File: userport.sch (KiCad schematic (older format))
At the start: 25 parts, among them CN10 USERPORT, U122 74LS654, U21 74LS04, U22 MOS_6529, U23 MOS_6551_ACIA, U28 GAL16V8, Y2 1.8432M

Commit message: Make JP12 a real jumper
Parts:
- JP12: footprint Jumper:SolderJumper-2_P1.3mm_Bridged_RoundedPad1.0x1.5mm -> Connector_PinHeader_2.54mm:PinHeader_1x02_P2.54mm_Vertical
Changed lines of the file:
@@
 F 0 "JP12" H 13840 1732 50  0000 C CNN
 F 1 "JP_TPSENSE" H 13840 1641 50  0000 C CNN
-F 2 "Jumper:SolderJumper-2_P1.3mm_Bridged_RoundedPad1.0x1.5mm" H 13840 1520 50  0001 C CNN
+F 2 "Connector_PinHeader_2.54mm:PinHeader_1x02_P2.54mm_Vertical" H 13840 1520 50  0001 C CNN
 F 3 "~" H 13840 1520 50  0001 C CNN
 	1    13840 1520

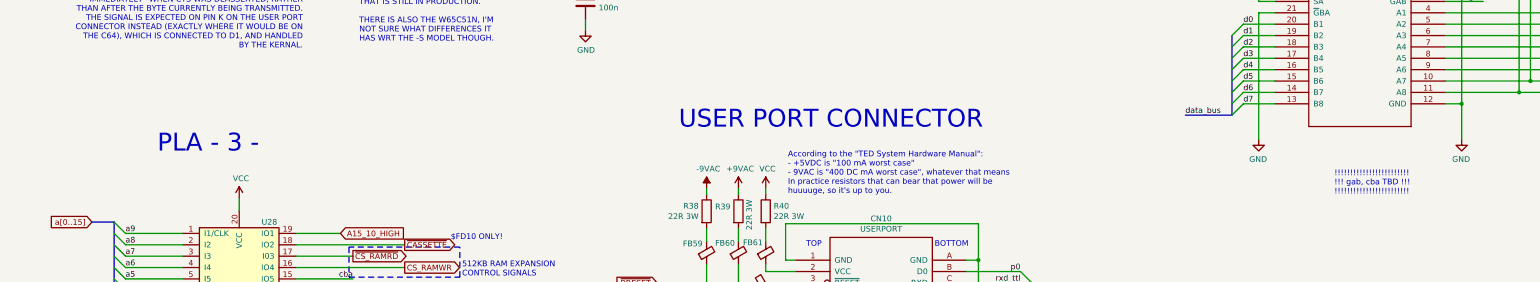
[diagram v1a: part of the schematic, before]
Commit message: Switch to 2-pin header for joyswap
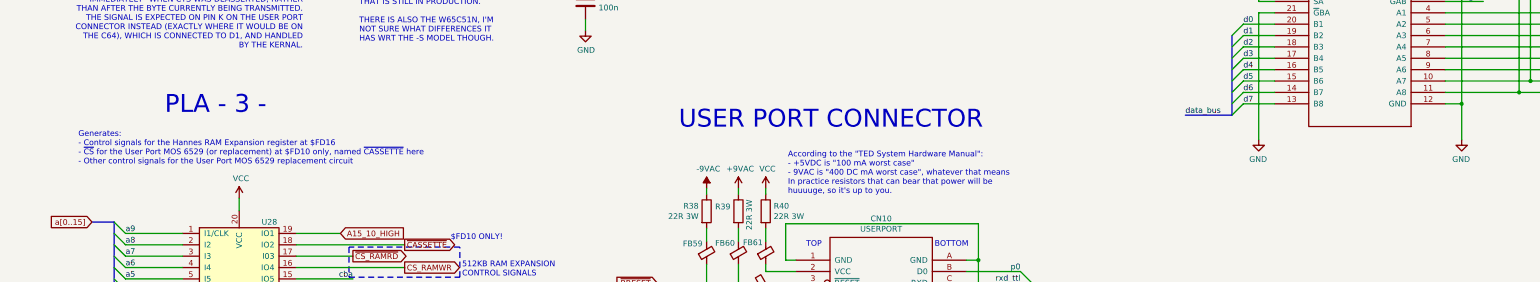
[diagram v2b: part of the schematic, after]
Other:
- note added: "Generates:\n- Control signals for the Hannes RAM Expansion register at $FD16\n- ~CS~ for the User Port MOS 6529 (or replacement) at $FD10 only, named ~CASSETTE~ here\n- Other control signals for the User Port MOS 6529 replacement circuit"
- note removed: "!!!!!!!!!!!!!!!!!!!!!!!!\n!!! gab, cba TBD !!!\n!!!!!!!!!!!!!!!!!!!!!!!!"
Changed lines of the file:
@@
 Text Label 9665 7530 2    50   ~ 0
 txd_ttl
-Text Notes 12425 5960 0    50   ~ 0
-!!!!!!!!!!!!!!!!!!!!!!!!\n!!! gab, cba TBD !!!\n!!!!!!!!!!!!!!!!!!!!!!!!
 Text Notes 8255 4200 0    50   ~ 0
 SOME CONTROL SIGNALS ARE INVERTED FOR\nHISTORICAL REASONS THAT DATE BACK TO\nTHE VIC-1011A
@@
 Text Label 3245 2925 0    50   ~ 0
 q-
-Text Notes 2075 5595 0    157  ~ 0
+Text Notes 2140 5255 0    157  ~ 0
 PLA - 3 -
 Text GLabel 3795 6495 2    50   Output ~ 0
@@
 Wire Bus Line
 	1695 6195 1695 7095
+Text Notes 1380 5695 0    50   ~ 0
+Generates:\n- Control signals for the Hannes RAM Expansion register at $FD16\n- ~CS~ for the User Port MOS 6529 (or replacement) at $FD10 only, named ~CASSETTE~ here\n- Other control signals for the User Port MOS 6529 replacement circuit
 $EndSCHEMATC

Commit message: U21 -> HCT
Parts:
- U21: value 74LS04 -> 74HCT04
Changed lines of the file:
@@
 P 8690 2745
 F 0 "U21" H 8690 2955 50  0000 C CNN
-F 1 "74LS04" H 8700 1605 50  0000 C CNN
+F 1 "74HCT04" H 8700 1605 50  0000 C CNN
 F 2 "LittleSixteen:DIP-14_W7.62mm_Socket_LongPads" H 8690 2745 50  0001 C CNN
 F 3 "http://www.ti.com/lit/gpn/sn74LS04" H 8690 2745 50  0001 C CNN
@@
 P 8690 2340
 F 0 "U21" H 8690 2565 50  0000 C CNN
-F 1 "74LS04" H 8690 2566 50  0001 C CNN
+F 1 "74HCT04" H 8690 2566 50  0001 C CNN
 F 2 "LittleSixteen:DIP-14_W7.62mm_Socket_LongPads" H 8690 2340 50  0001 C CNN
 F 3 "http://www.ti.com/lit/gpn/sn74LS04" H 8690 2340 50  0001 C CNN
@@
 P 8690 3210
 F 0 "U21" H 8690 3435 50  0000 C CNN
-F 1 "74LS04" H 8690 3436 50  0001 C CNN
+F 1 "74HCT04" H 8690 3436 50  0001 C CNN
 F 2 "LittleSixteen:DIP-14_W7.62mm_Socket_LongPads" H 8690 3210 50  0001 C CNN
 F 3 "http://www.ti.com/lit/gpn/sn74LS04" H 8690 3210 50  0001 C CNN
@@
 P 8690 3655
 F 0 "U21" H 8690 3880 50  0000 C CNN
-F 1 "74LS04" H 8690 3881 50  0001 C CNN
+F 1 "74HCT04" H 8690 3881 50  0001 C CNN
 F 2 "LittleSixteen:DIP-14_W7.62mm_Socket_LongPads" H 8690 3655 50  0001 C CNN
 F 3 "http://www.ti.com/lit/gpn/sn74LS04" H 8690 3655 50  0001 C CNN
@@
 P 11070 10770
 F 0 "U21" H 11070 11087 50  0000 C CNN
-F 1 "74LS04" H 11070 10996 50  0000 C CNN
+F 1 "74HCT04" H 11070 10996 50  0000 C CNN
 F 2 "LittleSixteen:DIP-14_W7.62mm_Socket_LongPads" H 11070 10770 50  0001 C CNN
 F 3 "http://www.ti.com/lit/gpn/sn74LS04" H 11070 10770 50  0001 C CNN
@@
 P 2975 10020
 F 0 "U21" H 3205 10066 50  0000 L CNN
-F 1 "74LS04" H 3205 9975 50  0000 L CNN
+F 1 "74HCT04" H 3205 9975 50  0000 L CNN
 F 2 "LittleSixteen:DIP-14_W7.62mm_Socket_LongPads" H 2975 10020 50  0001 C CNN
 F 3 "http://www.ti.com/lit/gpn/sn74LS04" H 2975 10020 50  0001 C CNN

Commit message: Rationalize BOM There should be no significant changes on both schematics on PCB, just some values and something on the silkscreen
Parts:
- C42, C43: MouserPN (none) -> 810-FG28X7R1H104KNT0
- FB59, FB60, FB61, FB62, FB63, FB64, FB65: value Ferrite_Bead_Small -> DSS1NB32A271Q91A; footprint LittleSixteen:Ferrite -> LittleSixteen:EMI_Filter; symbol ferrite_bead_small:Ferrite_Bead_Small -> emi_filter_3pin:EMI_Filter_3Pin
- JP12: value JP_TPSENSE -> JMP_TPSENSE
- R38, R39, R40: value 22R 3W -> 22 3W
- RP4: renamed from RN1; Notes (none) -> Bussed
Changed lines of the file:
@@
 d7
 $Comp
-L Device:R_Network08 RN1
+L Device:R_Network08 RP4
 U 1 1 63F3B9D0
 P 14350 3935
-F 0 "RN1" H 14738 3981 50  0000 L CNN
+F 0 "RP4" H 14738 3981 50  0000 L CNN
 F 1 "8.2k" H 14738 3890 50  0000 L CNN
 F 2 "Resistor_THT:R_Array_SIP9" V 14825 3935 50  0001 C CNN
 F 3 "http://www.vishay.com/docs/31509/csc.pdf" H 14350 3935 50  0001 C CNN
+F 4 "Bussed" H 14350 3935 50  0001 C CNN "Notes"
 	1    14350 3935
 	-1   0    0    -1
@@
 F 2 "Capacitor_THT:C_Disc_D8.0mm_W2.5mm_P5.00mm" H 2438 9890 50  0001 C CNN
 F 3 "~" H 2400 10040 50  0001 C CNN
+F 4 "810-FG28X7R1H104KNT0" H 2400 10040 50  0001 C CNN "MouserPN"
 	1    2400 10040
 	1    0    0    -1
@@
 	6905 7530 6905 6565
 $Comp
-L ferrite_bead_small:Ferrite_Bead_Small FB?
+L emi_filter_3pin:EMI_Filter_3Pin FB?
 U 1 1 647718B2
 P 7390 6730
@@
 AR Path="/63EAD078/647718B2" Ref="FB62"  Part="1"
 F 0 "FB62" V 7335 6595 50  0000 C CNN
-F 1 "Ferrite_Bead_Small" H 7490 6685 50  0001 L CNN
-F 2 "LittleSixteen:Ferrite" V 7320 6730 50  0001 C CNN
+F 1 "DSS1NB32A271Q91A" H 7490 6685 50  0001 L CNN
+F 2 "LittleSixteen:EMI_Filter" V 7320 6730 50  0001 C CNN
 F 3 "~" H 7390 6730 50  0001 C CNN
 	1    7390 6730
@@
 $EndComp
 $Comp
-L ferrite_bead_small:Ferrite_Bead_Small FB?
+L emi_filter_3pin:EMI_Filter_3Pin FB?
 U 1 1 6477BD12
 P 7185 6465
@@
 AR Path="/63EAD078/6477BD12" Ref="FB60"  Part="1"
 F 0 "FB60" H 6980 6380 50  0000 L CNN
-F 1 "Ferrite_Bead_Small" H 7285 6420 50  0001 L CNN
-F 2 "LittleSixteen:Ferrite" V 7115 6465 50  0001 C CNN
+F 1 "DSS1NB32A271Q91A" H 7285 6420 50  0001 L CNN
+F 2 "LittleSixteen:EMI_Filter" V 7115 6465 50  0001 C CNN
 F 3 "~" H 7185 6465 50  0001 C CNN
 	1    7185 6465
@@
 $EndComp
 $Comp
-L ferrite_bead_small:Ferrite_Bead_Small FB?
+L emi_filter_3pin:EMI_Filter_3Pin FB?
 U 1 1 64790452
 P 7455 7760
@@
 AR Path="/63EAD078/64790452" Ref="FB64"  Part="1"
 F 0 "FB64" H 7261 7760 50  0000 R CNN
-F 1 "Ferrite_Bead_Small" H 7555 7715 50  0001 L CNN
-F 2 "LittleSixteen:Ferrite" V 7385 7760 50  0001 C CNN
+F 1 "DSS1NB32A271Q91A" H 7555 7715 50  0001 L CNN
+F 2 "LittleSixteen:EMI_Filter" V 7385 7760 50  0001 C CNN
 F 3 "~" H 7455 7760 50  0001 C CNN
 	1    7455 7760
@@
 $EndComp
 $Comp
-L ferrite_bead_small:Ferrite_Bead_Small FB?
+L emi_filter_3pin:EMI_Filter_3Pin FB?
 U 1 1 647AEC6A
 P 9295 7760
@@
 AR Path="/63EAD078/647AEC6A" Ref="FB65"  Part="1"
 F 0 "FB65" H 9050 7685 50  0000 L CNN
-F 1 "Ferrite_Bead_Small" H 9395 7715 50  0001 L CNN
-F 2 "LittleSixteen:Ferrite" V 9225 7760 50  0001 C CNN
+F 1 "DSS1NB32A271Q91A" H 9395 7715 50  0001 L CNN
+F 2 "LittleSixteen:EMI_Filter" V 9225 7760 50  0001 C CNN
 F 3 "~" H 9295 7760 50  0001 C CNN
 	1    9295 7760
@@
 $EndComp
 $Comp
-L ferrite_bead_small:Ferrite_Bead_Small FB?
+L emi_filter_3pin:EMI_Filter_3Pin FB?
 U 1 1 647B8E58
 P 7425 6465
@@
 AR Path="/63EAD078/647B8E58" Ref="FB61"  Part="1"
 F 0 "FB61" H 7225 6375 50  0000 L CNN
-F 1 "Ferrite_Bead_Small" H 7525 6420 50  0001 L CNN
-F 2 "LittleSixteen:Ferrite" V 7355 6465 50  0001 C CNN
+F 1 "DSS1NB32A271Q91A" H 7525 6420 50  0001 L CNN
+F 2 "LittleSixteen:EMI_Filter" V 7355 6465 50  0001 C CNN
 F 3 "~" H 7425 6465 50  0001 C CNN
 	1    7425 6465
@@
 AR Path="/63EAD078/647C5CFF" Ref="R40"  Part="1"
 F 0 "R40" H 7495 6146 50  0000 L CNN
-F 1 "22R 3W" H 7495 6055 50  0000 L CNN
+F 1 "22 3W" H 7495 6055 50  0000 L CNN
 F 2 "Resistor_THT:R_Axial_DIN0414_L11.9mm_D4.5mm_P5.08mm_Vertical" V 7355 6100 50  0001 C CNN
 F 3 "~" H 7425 6100 50  0001 C CNN
@@
 	7490 7330 7690 7330
 $Comp
-L ferrite_bead_small:Ferrite_Bead_Small FB?
+L emi_filter_3pin:EMI_Filter_3Pin FB?
 U 1 1 6479A5EF
 P 7390 7330
@@
 AR Path="/63EAD078/6479A5EF" Ref="FB63"  Part="1"
 F 0 "FB63" V 7330 7195 50  0000 C CNN
-F 1 "Ferrite_Bead_Small" H 7490 7285 50  0001 L CNN
-F 2 "LittleSixteen:Ferrite" V 7320 7330 50  0001 C CNN
+F 1 "DSS1NB32A271Q91A" H 7490 7285 50  0001 L CNN
+F 2 "LittleSixteen:EMI_Filter" V 7320 7330 50  0001 C CNN
 F 3 "~" H 7390 7330 50  0001 C CNN
 	1    7390 7330
@@
 AR Path="/63EAD078/6486FE58" Ref="JP12"  Part="1"
 F 0 "JP12" H 13840 1732 50  0000 C CNN
-F 1 "JP_TPSENSE" H 13840 1641 50  0000 C CNN
+F 1 "JMP_TPSENSE" H 13840 1641 50  0000 C CNN
 F 2 "Connector_PinHeader_2.54mm:PinHeader_1x02_P2.54mm_Vertical" H 13840 1520 50  0001 C CNN
 F 3 "~" H 13840 1520 50  0001 C CNN
@@
 ~TAPE_SENSE
 $Comp
-L ferrite_bead_small:Ferrite_Bead_Small FB?
+L emi_filter_3pin:EMI_Filter_3Pin FB?
 U 1 1 647EB007
 P 6905 6465
@@
 AR Path="/63EAD078/647EB007" Ref="FB59"  Part="1"
 F 0 "FB59" H 6870 6385 50  0000 R CNN
-F 1 "Ferrite_Bead_Small" H 7005 6420 50  0001 L CNN
-F 2 "LittleSixteen:Ferrite" V 6835 6465 50  0001 C CNN
+F 1 "DSS1NB32A271Q91A" H 7005 6420 50  0001 L CNN
+F 2 "LittleSixteen:EMI_Filter" V 6835 6465 50  0001 C CNN
 F 3 "~" H 6905 6465 50  0001 C CNN
 	1    6905 6465
@@
 AR Path="/63EAD078/64956DD2" Ref="R38"  Part="1"
 F 0 "R38" H 6835 6146 50  0000 R CNN
-F 1 "22R 3W" H 6835 6055 50  0000 R CNN
+F 1 "22 3W" H 6835 6055 50  0000 R CNN
 F 2 "Resistor_THT:R_Axial_DIN0414_L11.9mm_D4.5mm_P5.08mm_Vertical" V 6835 6100 50  0001 C CNN
 F 3 "~" H 6905 6100 50  0001 C CNN
@@
 AR Path="/63EAD078/64956726" Ref="R39"  Part="1"
 F 0 "R39" H 6980 6140 50  0000 L CNN
-F 1 "22R 3W" V 7280 5935 50  0000 L CNN
+F 1 "22 3W" V 7280 5935 50  0000 L CNN
 F 2 "Resistor_THT:R_Axial_DIN0414_L11.9mm_D4.5mm_P5.08mm_Vertical" V 7115 6100 50  0001 C CNN
 F 3 "~" H 7185 6100 50  0001 C CNN
@@
 F 2 "Capacitor_THT:C_Disc_D8.0mm_W2.5mm_P5.00mm" H 898 9890 50  0001 C CNN
 F 3 "~" H 860 10040 50  0001 C CNN
+F 4 "810-FG28X7R1H104KNT0" H 860 10040 50  0001 C CNN "MouserPN"
 	1    860  10040
 	1    0    0    -1

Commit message: Rationalize capacitor footprints & BOM
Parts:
- CN10: MouserPN (none) -> ---
- R41, R42: MouserPN (none) -> 603-MFR-25FTF52-10K
- U22: MouserPN (none) -> :)
- U23: MouserPN (none) -> :); Notes (none) -> Or MOS 8551, WDC W65C51S (Maybe -N too), Rockwell R6551(A)P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
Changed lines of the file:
@@
 F 2 "LittleSixteen:DIP-20_W7.62mm_Socket_LongPads" H 12650 1800 50  0001 C CNN
 F 3 "DOCUMENTATION" H 12650 1800 50  0001 C CNN
+F 4 ":)" H 12650 1800 50  0001 C CNN "MouserPN"
 	1    12650 1800
 	-1   0    0    -1
@@
 F 2 "LittleSixteen:Plus4_UserPort" H 8440 7080 50  0001 C CNN
 F 3 "DOCUMENTATION" H 8440 7080 50  0001 C CNN
+F 4 "---" H 8440 7080 50  0001 C CNN "MouserPN"
 	1    8440 7080
 	1    0    0    -1
@@
 F 2 "LittleSixteen:DIP-28_W15.24mm_Socket_LongPads" H 4490 2975 50  0001 C CNN
 F 3 "DOCUMENTATION" H 4490 2975 50  0001 C CNN
+F 4 ":)" H 4490 2975 50  0001 C CNN "MouserPN"
+F 5 "Or MOS 8551, WDC W65C51S (Maybe -N too), Rockwell R6551(A)P, UMC UM6551(A)" H 4490 2975 50  0001 C CNN "Notes"
 	1    4490 2975
 	1    0    0    -1
@@
 F 2 "LittleSixteen:DIP-20_W7.62mm_Socket_LongPads" H 1435 10040 50  0001 C CNN
 F 3 "DOCUMENTATION" H 1435 10040 50  0001 C CNN
+F 4 ":)" H 1435 10040 50  0001 C CNN "MouserPN"
 	2    1435 10040
 	1    0    0    -1
@@
 F 2 "Resistor_THT:R_Axial_DIN0207_L6.3mm_D2.5mm_P5.08mm_Vertical" V 9520 2870 50  0001 C CNN
 F 3 "~" H 9590 2870 50  0001 C CNN
+F 4 "603-MFR-25FTF52-10K" H 9590 2870 50  0001 C CNN "MouserPN"
 	1    9590 2870
 	1    0    0    -1
@@
 F 2 "Resistor_THT:R_Axial_DIN0207_L6.3mm_D2.5mm_P5.08mm_Vertical" V 9870 2870 50  0001 C CNN
 F 3 "~" H 9940 2870 50  0001 C CNN
+F 4 "603-MFR-25FTF52-10K" H 9940 2870 50  0001 C CNN "MouserPN"
 	1    9940 2870
 	1    0    0    -1

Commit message: Add note on some components
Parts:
- Y2: Notes (none) -> Series, no load cap, max series resistance: 400R
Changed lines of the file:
@@
 F 2 "Crystal:Crystal_HC49-U_Vertical" H 2685 2705 50  0001 C CNN
 F 3 "~" H 2685 2705 50  0001 C CNN
+F 4 "Series, no load cap, max series resistance: 400R" H 2685 2705 50  0001 C CNN "Notes"
 	1    2685 2705
 	0    -1   -1   0
